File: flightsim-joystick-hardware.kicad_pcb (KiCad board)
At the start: 2 copper layers, 43.2 x 22.1 mm, 17 parts, among them J1 USB_OTG, J2 Conn_01x02, J3 Conn_01x02, P1 CONN_02X03, U1 ATMEGA328P-AU, Y1 12MHz

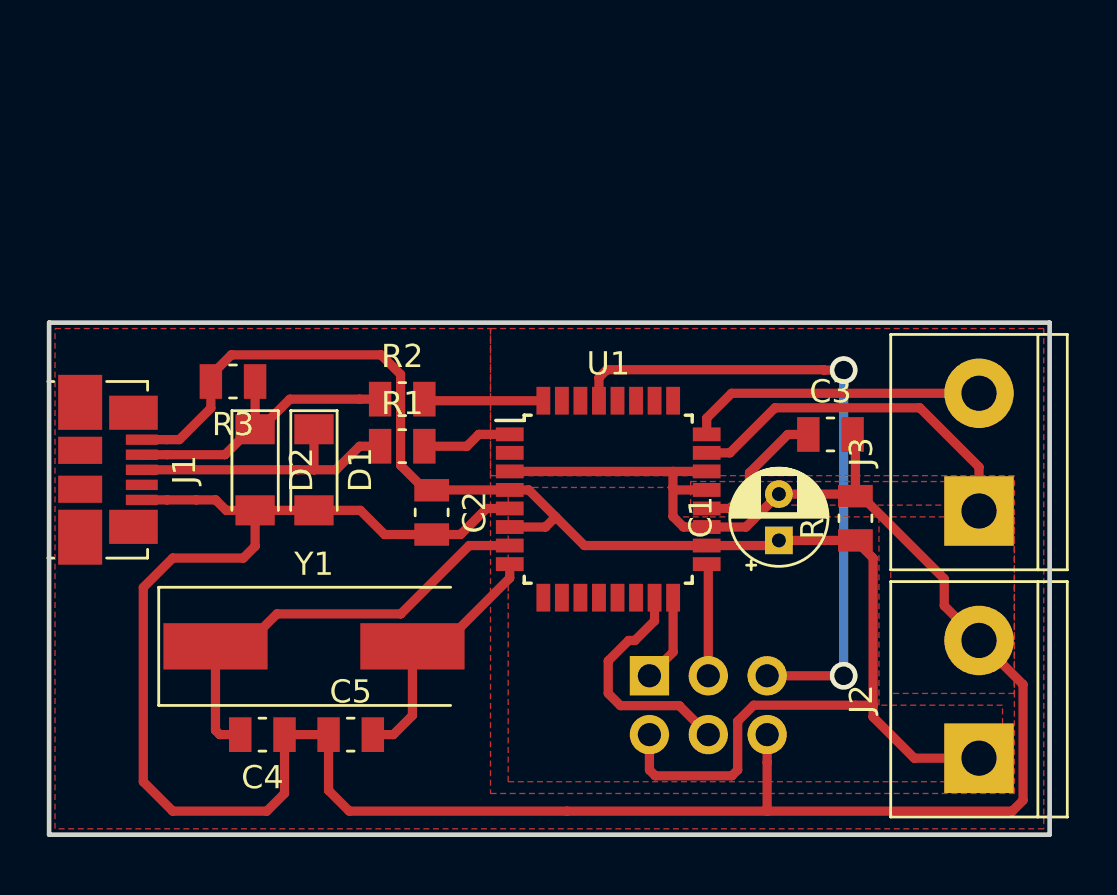
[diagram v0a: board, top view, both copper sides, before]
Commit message: add 2 more ADC connectors
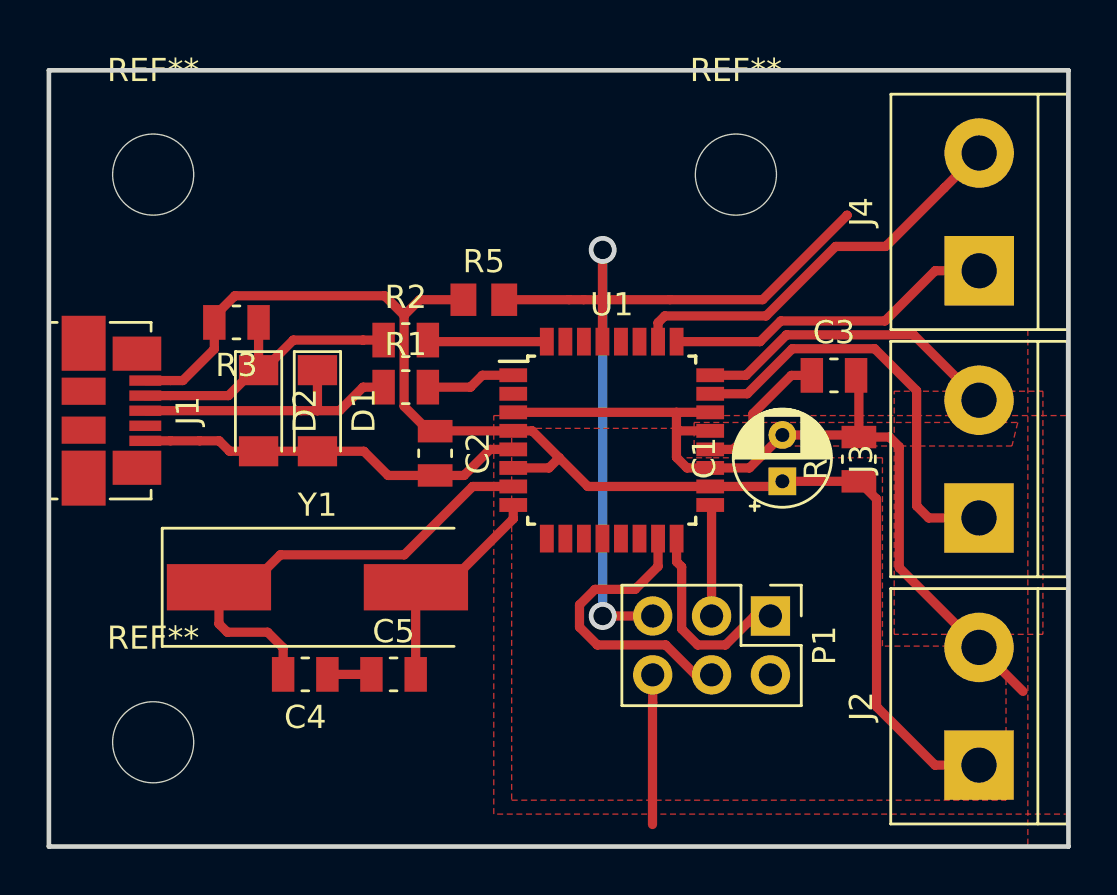
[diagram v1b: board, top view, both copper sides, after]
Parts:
- added G***: LOGO, Logo:logo_didee, B.Cu at (84.3, 91.0)
- added J4: Conn_01x02, TerminalBlock:TerminalBlock_bornier-2_P5.08mm, F.Cu at (107.5, 82.8)
- added R5: 10k, Resistor_SMD:R_0805_2012Metric, F.Cu at (86.1, 84.1)
- added REF**: MountingHole_3.5mm, MountingHole:MountingHole_3.5mm, F.Cu at (97.0, 78.7)
- added REF**: MountingHole_3.5mm, MountingHole:MountingHole_3.5mm, F.Cu at (71.8, 103.2)
- added REF**: MountingHole_3.5mm, MountingHole:MountingHole_3.5mm, F.Cu at (71.8, 78.7)
- P1: moved to F.Cu
- moved P1 5.82 mm to (98.4, 97.8)
- moved C4 3.19 mm to (78.4, 100.3)
- moved C5 3.19 mm to (82.2, 100.3)
- moved R1 2.55 mm to (82.7, 87.9)
- moved C1 2.55 mm to (99.0, 91.9)
- moved C2 2.55 mm to (84.0, 90.7)
- moved D1 2.55 mm to (78.9, 88.9)
- moved J1 2.55 mm to (70.0, 88.9)
- moved R2 2.55 mm to (82.7, 85.8)
- moved U1 2.55 mm to (91.6, 90.2)
- moved Y1 2.55 mm to (78.9, 96.5)
- moved C3 2.55 mm to (101.2, 87.4)
- moved D2 2.55 mm to (76.3, 88.9)
- moved R3 2.55 mm to (75.4, 85.1)
- moved R4 2.55 mm to (102.3, 91.0)
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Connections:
- U1 pad 25: (no net) -> /Z_Pos
- U1 pad 26: (no net) -> /W_Pos
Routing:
- net GND: track 120.0 -> 63.9 mm
- net /W_Pos: track 0.00 -> 17.7 mm
- net /Z_Pos: track 0.00 -> 14.3 mm
- net Net-(P1-Pad5): track 28.2 -> 38.8 mm
- net +5V: track 68.1 -> 59.5 mm
- net Net-(P1-Pad1): track 3.79 -> 8.62 mm
- net /X_Pos: track 15.5 -> 18.3 mm
- net Net-(P1-Pad4): track 10.2 -> 12.8 mm
- net Net-(C5-Pad2): track 11.1 -> 9.79 mm
- net Net-(C4-Pad2): track 19.3 -> 20.4 mm
- net /Y_Pos: track 12.9 -> 13.5 mm
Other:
- board size 43.2 x 22.1 mm -> 44 x 33.5 mm
